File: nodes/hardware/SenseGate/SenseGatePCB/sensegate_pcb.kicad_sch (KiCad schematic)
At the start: 11 parts, among them J1 Conn_01x04_Socket, J2 Conn_01x04_Socket, J3 Conn_01x04_Socket, J4 Conn_01x24_Pin, J5 Conn_01x04_Socket, SW1 SW_Reed, SW2 SW_Reed, SW3 SW_Reed, U1 DD05CVSA

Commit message: wip schematic and pcb
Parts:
- removed J1, J2, J3: Conn_01x04_Socket, symbol Connector:Conn_01x04_Socket
- added J1, J10, J11: Conn_01x02_Pin, symbol Connector:Conn_01x02_Pin
- added J2, J3, J9: Conn_01x02_Socket, symbol Connector:Conn_01x02_Socket
- added J6, J7, J8: Conn_01x04_Socket, Connector_JST:JST_PH_B4B-PH-K_1x04_P2.00mm_Vertical, symbol Connector:Conn_01x04_Socket
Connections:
- net GND: now reaches J5.2 (Pin_2)
- net GND: now also J4.GND (Pin_22), U1.5 (GND)
- net 20V: now reaches J5.3 (Pin_3)
- net IS_ADC: now reaches J5.4 (Pin_4)
- net IS_ADC: now also J4.P0.02_A0_D0_/_BUZ_EN (Pin_1)
- net at SC1.1 (+): now also J10.2 (Pin_2); no longer U1.1 (VIN)
- net at SC1.2 (-): now also J10.1 (Pin_1); no longer U1.2 (GND)
- net at U1.3 (Bat+): now also J9.2 (Pin_2); no longer BT1.1 (+)
- net at U1.4 (GND(bat-)): now also J9.1 (Pin_1); no longer BT1.2 (-)
- net VBAT: now reaches U1.6 (VOUT)
- net VBAT: now also J4.VBAT (Pin_24)
- new net: J3.1 (Pin_1), U1.2 (GND)
- new net: J3.2 (Pin_2), U1.1 (VIN)
- new net: BT1.1 (+), J11.2 (Pin_2)
- new net: BT1.2 (-), J11.1 (Pin_1)
- new net +3V3: J4.+3V3 (Pin_21), J6.4 (Pin_4), J7.4 (Pin_4), J8.4 (Pin_4)
- new net reed_sw_01_measure: J4.P0.09_D14_/_TMB2 (Pin_8), J8.3 (Pin_3)
- new net reed_sw_02_measure: J4.P1.01_D13_/_TMBT1 (Pin_6), J6.3 (Pin_3)
- new net reed_sw_03_measure: J4.P0.19_D12_/_TMB1 (Pin_4), J7.3 (Pin_3)
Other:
- moved on the sheet: BT1, J4, SC1

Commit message: sensegate pcb wip
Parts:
- added BT2: Battery, Connector_JST:JST_PH_S2B-PH-K_1x02_P2.00mm_Horizontal, symbol Device:Battery
- added Q4: SS8050, Package_TO_SOT_SMD:SOT-23, symbol Transistor_BJT:SS8050
- added R3, R4, R5, R6, R7: R, Resistor_SMD:R_0805_2012Metric, symbol Device:R
- added SW5: SW_DPDT_x2, SenseMateLibrary:OS102011MA1QN1, symbol Switch:SW_DPDT_x2
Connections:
- net +3V3: now also J6.3 (Pin_3), J7.3 (Pin_3), J8.3 (Pin_3); no longer J6.4 (Pin_4), J7.4 (Pin_4), J8.4 (Pin_4)
- net GND: now also BT2.2 (-), R7.1
- net IS_ADC: now also R6.1, R7.2; no longer J5.4 (Pin_4)
- net VBAT: now also SW5.1 (A)
- net reed_sw_01_measure: now also J8.4 (Pin_4); no longer J8.3 (Pin_3)
- net reed_sw_02_measure: now also J6.4 (Pin_4); no longer J6.3 (Pin_3)
- net reed_sw_03_measure: now also J7.4 (Pin_4); no longer J7.3 (Pin_3)
- net at J3.1 (Pin_1), U1.2 (GND): now also R4.1
- net at J3.2 (Pin_2), U1.1 (VIN): now also R5.1
- net MON_SOLAR: now reaches J4.P0.05_A5_D5_/_SCL (Pin_11)
- net MON_SOLAR: now also R4.2, R5.2
- net TOG_20V: now reaches J4.P0.10_D15_/_VIB_EN (Pin_10)
- net TOG_20V: now also R3.2
- new net: Q4.1 (B), R3.1
- new net: J5.4 (Pin_4), R6.2
- new net: BT2.1 (+), SW5.2 (B)
- no-connect marks 0 -> 1
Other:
- note added: "Spannungsteiler für 7V -> 3,3V"
- moved on the sheet: BT1, J1, J10, J11, J2, J3, J4, J5, J9, SC1, U1

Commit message: schematic done
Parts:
- removed BT1: Battery_Cell, symbol Device:Battery_Cell
- removed J11: Conn_01x02_Pin, symbol Connector:Conn_01x02_Pin
- removed J9: Conn_01x02_Socket, symbol Connector:Conn_01x02_Socket
- added C1, C2: C, symbol Device:C
- added J9: Conn_01x04_Socket, Connector_JST:JST_PH_B4B-PH-K_1x04_P2.00mm_Vertical, symbol Connector:Conn_01x04_Socket
- added R10, R11, R12, R13, R14, R15, R8, R9: R, Resistor_SMD:R_0805_2012Metric, symbol Device:R
- added RV1: R_Potentiometer, symbol Device:R_Potentiometer
- added U2: mt3608_dcdc_converter, custom_dcdc_converters:MT3608_solarbotics, symbol custom_symbols:mt3608_dcdc_converter
- J3: footprint (none) -> Connector_JST:JST_PH_B2B-PH-K_1x02_P2.00mm_Vertical
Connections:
- net +3V3: now also J9.3 (Pin_3), R10.1, R12.1, R14.1, R8.1
- net 20V: now also U2.1 (VOUT+)
- net GND: now also J6.2 (Pin_2), J7.2 (Pin_2), J8.2 (Pin_2), U1.4 (GND(bat-)), C2.2, J9.2 (Pin_2), R11.2, R13.2, R15.2, R9.2, RV1.3, U2.4 (VIN-); no longer J5.2 (Pin_2)
- net IS_ADC: now also RV1.2
- net MON_SOLAR: now also C1.1
- net VBAT: now also Q4.3 (C), U1.3 (Bat+), C2.1
- net reed_sw_01_measure: now also R10.2, R11.1
- net reed_sw_02_measure: now also R12.2, R13.1
- net reed_sw_03_measure: now also R14.2, R15.1
- net at Q4.2 (E): now also U2.3 (VIN+)
- net at J5.4 (Pin_4), R6.2: now also RV1.1
- net at J3.1 (Pin_1), R4.1, U1.2 (GND): now also C1.2
- net reed_sw_04_measure: now reaches J4.P0.04_A4_D4_/_SDA (9)
- net reed_sw_04_measure: now also J9.4 (Pin_4), R8.2, R9.1
- new net GND_IS: J5.2 (Pin_2), U2.2 (VOUT-)
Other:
- note added: "Schalter aus -> Akku laden aus"
- moved on the sheet: J10, J3, J5, J6, J7, J8, Q4, R3, R5, R6, R7, SC1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

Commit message: wip
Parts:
- removed J1: Conn_01x02_Pin, symbol Connector:Conn_01x02_Pin
- removed J2: Conn_01x02_Socket, symbol Connector:Conn_01x02_Socket
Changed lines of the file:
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@@
 	(wire
 		(pts
-			(xy 146.05 62.23) (xy 154.94 62.23)
+			(xy 151.13 62.23) (xy 154.94 62.23)
 		)
 		(stroke
@@
 	(global_label "VBAT"
 		(shape input)
-		(at 146.05 62.23 180)
+		(at 151.13 62.23 180)
 		(fields_autoplaced yes)
 		(effects
@@
 		)
 		(property "Intersheetrefs" "${INTERSHEET_REFS}"
-			(at 138.65 62.23 0)
+			(at 143.73 62.23 0)
 			(hide yes)
 			(show_name no)
@@
 	)
 	(symbol
-		(lib_id "Connector:Conn_01x02_Pin")
-		(at 215.9 33.02 0)
-		(unit 1)
-		(body_style 1)
-		(exclude_from_sim no)
-		(in_bom yes)
-		(on_board yes)
-		(in_pos_files yes)
-		(dnp no)
-		(fields_autoplaced yes)
-		(property "Reference" "J1"
-			(at 216.535 27.94 0)
-			(show_name no)
-			(do_not_autoplace no)
-			(effects
-				(font
-					(size 1.27 1.27)
-				)
-			)
-		)
-		(property "Value" "Conn_01x02_Pin"
-			(at 216.535 30.48 0)
-			(show_name no)
-			(do_not_autoplace no)
-			(effects
-				(font
-					(size 1.27 1.27)
-				)
-			)
-		)
-		(property "Footprint" ""
-			(at 215.9 33.02 0)
-			(hide yes)
-			(show_name no)
-			(do_not_autoplace no)
-			(effects
-				(font
-					(size 1.27 1.27)
-				)
-			)
-		)
-		(property "Datasheet" ""
-			(at 215.9 33.02 0)
-			(hide yes)
-			(show_name no)
-			(do_not_autoplace no)
-			(effects
-				(font
-					(size 1.27 1.27)
-				)
-			)
-		)
-		(property "Description" "Generic connector, single row, 01x02, script generated"
-			(at 215.9 33.02 0)
-			(hide yes)
-			(show_name no)
-			(do_not_autoplace no)
-			(effects
-				(font
-					(size 1.27 1.27)
-				)
-			)
-		)
-		(pin "1"
-		)
-		(pin "2"
-		)
-		(instances
-			(project "sensegate_pcb"
-				(path "/cab49cbb-a41f-4356-a83b-79a7aa8374de"
-					(reference "J1")
-					(unit 1)
-				)
-			)
-		)
-	)
-	(symbol
 		(lib_id "custom_symbols:mt3608_dcdc_converter")
 		(at 91.44 170.18 0)
@@
 					(unit 1)
 				)
-			)
-		)
-	)
-	(symbol
-		(lib_id "Connector:Conn_01x02_Socket")
-		(at 234.95 35.56 180)
-		(unit 1)
-		(body_style 1)
-		(exclude_from_sim no)
-		(in_bom yes)
-		(on_board yes)
-		(in_pos_files yes)
-		(dnp no)
-		(fields_autoplaced yes)
-		(property "Reference" "J2"
-			(at 235.585 27.94 0)
-			(show_name no)
-			(do_not_autoplace no)
-			(effects
-				(font
-					(size 1.27 1.27)
-				)
-			)
-		)
-		(property "Value" "Conn_01x02_Socket"
-			(at 235.585 30.48 0)
-			(show_name no)
-			(do_not_autoplace no)
-			(effects
-				(font
-					(size 1.27 1.27)
-				)
-			)
-		)
-		(property "Footprint" ""
-			(at 234.95 35.56 0)
-			(hide yes)
-			(show_name no)
-			(do_not_autoplace no)
-			(effects
-				(font
-					(size 1.27 1.27)
-				)
-			)
-		)
-		(property "Datasheet" ""
-			(at 234.95 35.56 0)
-			(hide yes)
-			(show_name no)
-			(do_not_autoplace no)
-			(effects
-				(font
-					(size 1.27 1.27)
-				)
-			)
-		)
-		(property "Description" "Generic connector, single row, 01x02, script generated"
-			(at 234.95 35.56 0)
-			(hide yes)
-			(show_name no)
-			(do_not_autoplace no)
-			(effects
-				(font
-					(size 1.27 1.27)
-				)
-			)
-		)
-		(pin "1"
-		)
-		(pin "2"
-		)
-		(instances
-			(project "sensegate_pcb"
-				(path "/cab49cbb-a41f-4356-a83b-79a7aa8374de"
-					(reference "J2")
-					(unit 1)
-				)

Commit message: sensegate pcb v1 done?!
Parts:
- C1, C2: footprint (none) -> Capacitor_THT:CP_Axial_L10.0mm_D6.0mm_P15.00mm_Horizontal
- RV1: footprint (none) -> Potentiometer_THT:Potentiometer_Bourns_3266W_Vertical
- SW5: footprint SenseMateLibrary:OS102011MA1QN1 -> SenseGateLib:OS102011MA1QN1
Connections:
- net GND: no longer U1.5 (GND)
- net VBAT: no longer U1.6 (VOUT)
- no-connect marks 1 -> 3
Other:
- moved on the sheet: BT2, C1, C2, J10, J3, J4, J5, J6, J7, J8, J9, Q4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

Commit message: changed c1 and c2 capacitor type to 0805 ceramic
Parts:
- C1, C2: footprint Capacitor_THT:CP_Axial_L10.0mm_D6.0mm_P15.00mm_Horizontal -> Capacitor_SMD:C_0805_2012Metric
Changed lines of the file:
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@@
 			)
 		)
-		(property "Footprint" "Capacitor_THT:CP_Axial_L10.0mm_D6.0mm_P15.00mm_Horizontal"
+		(property "Footprint" "Capacitor_SMD:C_0805_2012Metric"
 			(at 168.6052 53.34 0)
 			(hide yes)
@@
 			)
 		)
-		(property "Footprint" "Capacitor_THT:CP_Axial_L10.0mm_D6.0mm_P15.00mm_Horizontal"
+		(property "Footprint" "Capacitor_SMD:C_0805_2012Metric"
 			(at 186.3852 104.14 0)
 			(hide yes)

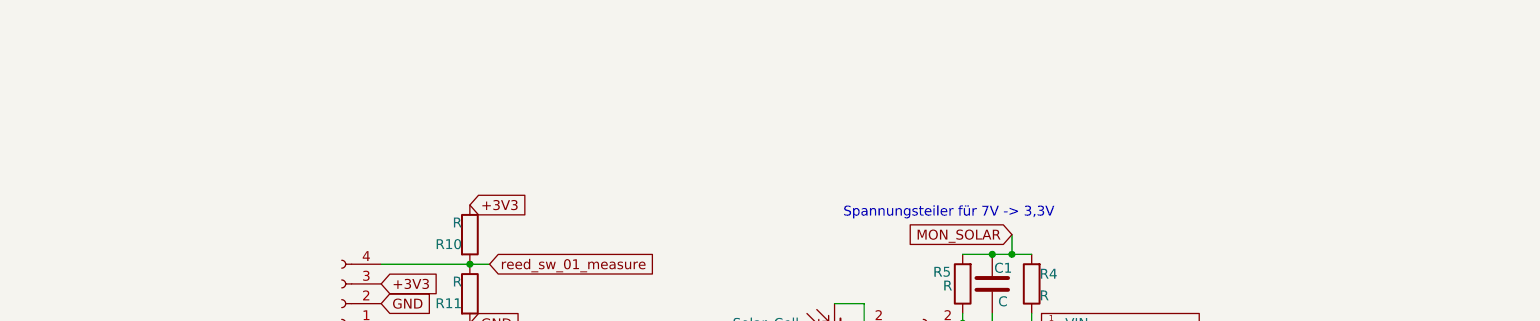
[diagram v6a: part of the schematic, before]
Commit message: mounting holes for battery added and add schematic for 7.8mm holes
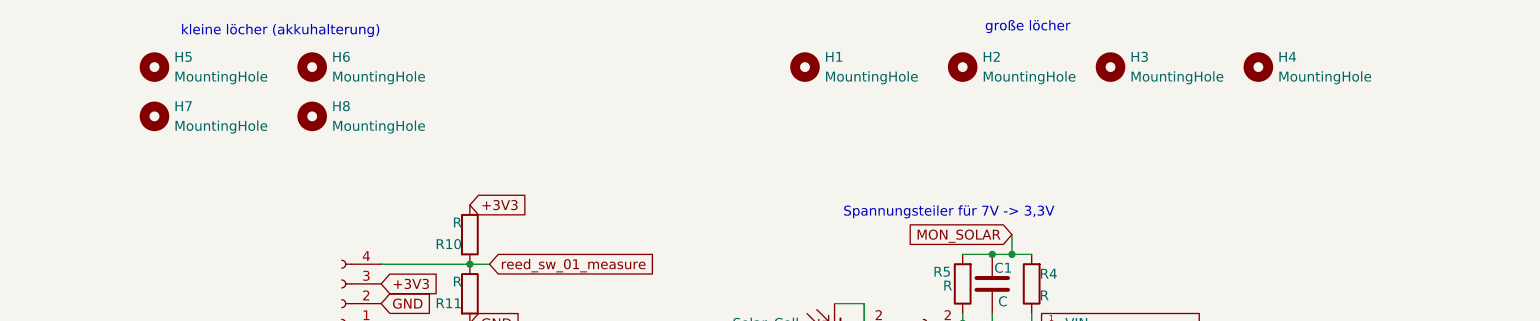
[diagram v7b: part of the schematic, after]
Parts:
- added H1, H2, H3, H4: MountingHole, SenseGateLib:mounting_hole_7.8mm, symbol Mechanical:MountingHole
- added H5, H6, H7, H8: MountingHole, MountingHole:MountingHole_2.2mm_M2, symbol Mechanical:MountingHole
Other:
- note added: "große löcher"
- note added: "kleine löcher (akkuhalterung)"
